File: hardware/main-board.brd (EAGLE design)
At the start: 160 x 100 mm, 1 part, among them U1 ESP32-D0WDQ6

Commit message: added build folder to .gitignore
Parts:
- added C1, C2: 0.1uF, SparkFun-Capacitors:0603
- added C10: 10nF, SparkFun-Capacitors:0603
- added C3: 1.0uF, SparkFun-Capacitors:0603
- added C4, C7: 0.1uF, SparkFun-Capacitors:0402
- added C5, C8: 1.0uF, SparkFun-Capacitors:0402
- added C6: 10uF, SparkFun-Capacitors:0805
- added C9: 100PF, SparkFun-Capacitors:0402
- added IC1, IC2: SI1147, silabs:QFN-10
- added L1: 2.7nH/?%/900mA/70mOhm, SparkFun-Coils:0402-TIGHT
- moved U1 18.3 mm to (10.2, 16.5)
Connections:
- removed net VDD3P3: U1.3, U1.4
- removed net VDD3P3_CPU: U1.37
- removed net VDD3P3_RTC: U1.19
- removed net VDDA: U1.1, U1.43, U1.46
- removed net VDD_SDIO: U1.26
- new net 3.3V: C1.1, C2.1, C3.1, C4.1, C5.1, C6.1, L1.1, U1.19, U1.26, U1.37
- new net 3.3V_SENSOR_1: IC1.3, U1.23
- new net 3.3V_SENSOR_2: IC2.3, U1.24
- new net N$1: C10.1, U1.48
- new net N$2: C7.1, C8.1, C9.1, U1.1, U1.43, U1.46
- new net N$3: L1.2, U1.3, U1.4
- new net PROX_INT_1: IC1.4
- new net PROX_INT_2: IC2.4
- new net SCL: IC1.2, IC2.2, U1.22
- new net SDA: IC1.1, IC2.1, U1.21
- new net SPKR_NEG: U1.15
- new net SPKR_POS: U1.14
- net GND: now also C1.2, C10.2, C2.2, C3.2, C4.2, C5.2, C6.2, C7.2, C8.2, C9.2, IC1.8, IC2.8

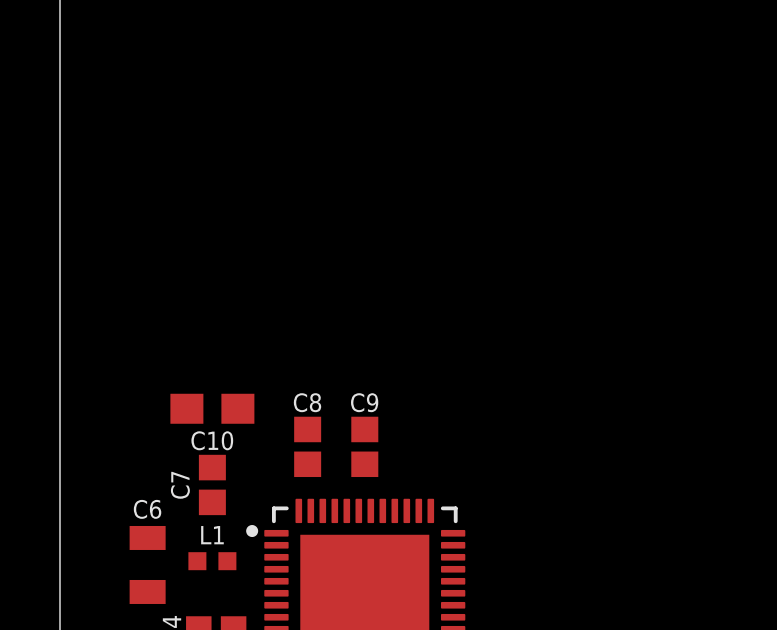
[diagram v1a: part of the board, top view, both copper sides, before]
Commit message: added tx/rx pins for programming
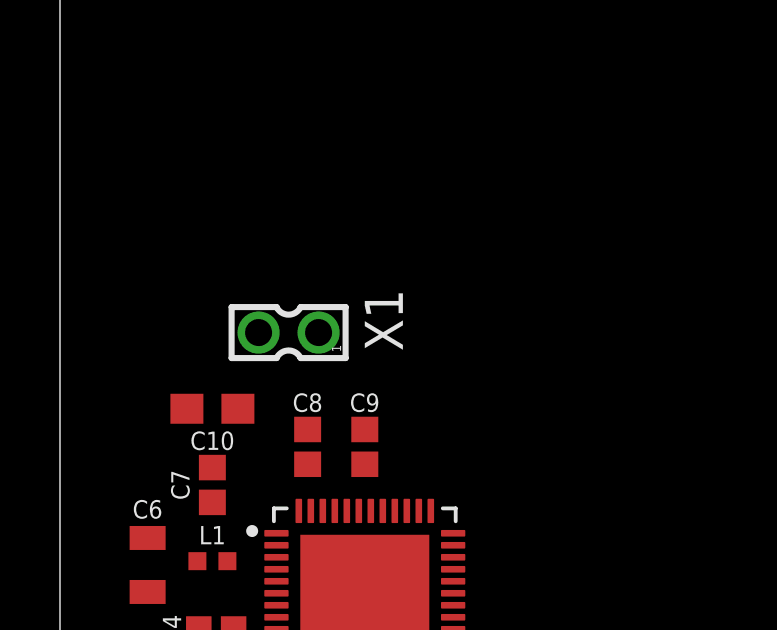
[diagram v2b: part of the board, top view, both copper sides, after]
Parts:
- added X1: 87758-0216, con-molex:87758-0216
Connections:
- new net PROG_RX: U1.40, X1.1
- new net PROG_TX: U1.41, X1.2
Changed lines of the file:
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@@
 <attribute name="NAME" x="21.36" y="3.83" size="1.27" layer="25" rot="R90"/>
 <attribute name="POPULARITY" value="0" x="22.86" y="5.08" size="1.778" layer="27" rot="R90" display="off"/>
-<attribute name="VALUE" x="25.86" y="3.83" size="1.27" layer="27" rot="R90"/>
 </element>
 <element name="IC2" library="silabs" library_urn="urn:adsk.eagle:library:358" package="QFN-10" package3d_urn="urn:adsk.eagle:package:26384/1" value="SI1147" x="3.81" y="5.08" smashed="yes" rot="R90">
 <attribute name="NAME" x="2.31" y="3.83" size="1.27" layer="25" rot="R90"/>
 <attribute name="POPULARITY" value="0" x="3.81" y="5.08" size="1.778" layer="27" rot="R90" display="off"/>
-<attribute name="VALUE" x="6.81" y="3.83" size="1.27" layer="27" rot="R90"/>
 </element>
 <element name="C1" library="SparkFun-Capacitors" package="0603" value="0.1uF" x="11.43" y="11.43" smashed="yes">
@@
 <attribute name="PROD_ID" value="CAP-00867" x="5.08" y="22.86" size="1.778" layer="27" rot="R180" display="off"/>
 <attribute name="VALUE" x="5.08" y="23.622" size="0.6096" layer="27" font="vector" ratio="20" rot="R180" align="top-center"/>
+</element>
+<element name="X1" library="con-molex" library_urn="urn:adsk.eagle:library:165" package="87758-0216" package3d_urn="urn:adsk.eagle:package:8078894/1" value="87758-0216" x="7.62" y="25.4" smashed="yes" rot="R90">
+<attribute name="MF" value="MOLEX" x="7.62" y="25.4" size="1.778" layer="27" rot="R90" display="off"/>
+<attribute name="MPN" value="87758-0216" x="7.62" y="25.4" size="1.778" layer="27" rot="R90" display="off"/>
+<attribute name="NAME" x="11.43" y="24.78" size="1.27" layer="25" rot="R90"/>
+<attribute name="OC_FARNELL" value="unknown" x="7.62" y="25.4" size="1.778" layer="27" rot="R90" display="off"/>
+<attribute name="OC_NEWARK" value="94M1513" x="7.62" y="25.4" size="1.778" layer="27" rot="R90" display="off"/>
+<attribute name="POPULARITY" value="4" x="7.62" y="25.4" size="1.778" layer="27" rot="R90" display="off"/>
 </element>
 </elements>
@@
 <wire x1="5.93" y1="22.86" x2="7.96" y2="19.455" width="0" layer="19" extent="1-1"/>
 </signal>
+<signal name="PROG_RX">
+<contactref element="U1" pad="40"/>
+<contactref element="X1" pad="1"/>
+<wire x1="8.62" y1="25.4" x2="11.16" y2="19.455" width="0" layer="19" extent="1-1"/>
+</signal>
+<signal name="PROG_TX">
+<contactref element="U1" pad="41"/>
+<contactref element="X1" pad="2"/>
+<wire x1="6.62" y1="25.4" x2="10.76" y2="19.455" width="0" layer="19" extent="1-1"/>
+</signal>
 </signals>
